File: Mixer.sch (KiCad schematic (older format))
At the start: 53 parts, among them J1 JST XH, J10 JST XH, J11 JST XH, J12 Conn_01x03_Female, J2 JST XH, J3 JST XH, J4 JST XH, J5 JST XH, J6 JST XH, J7 JST XH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

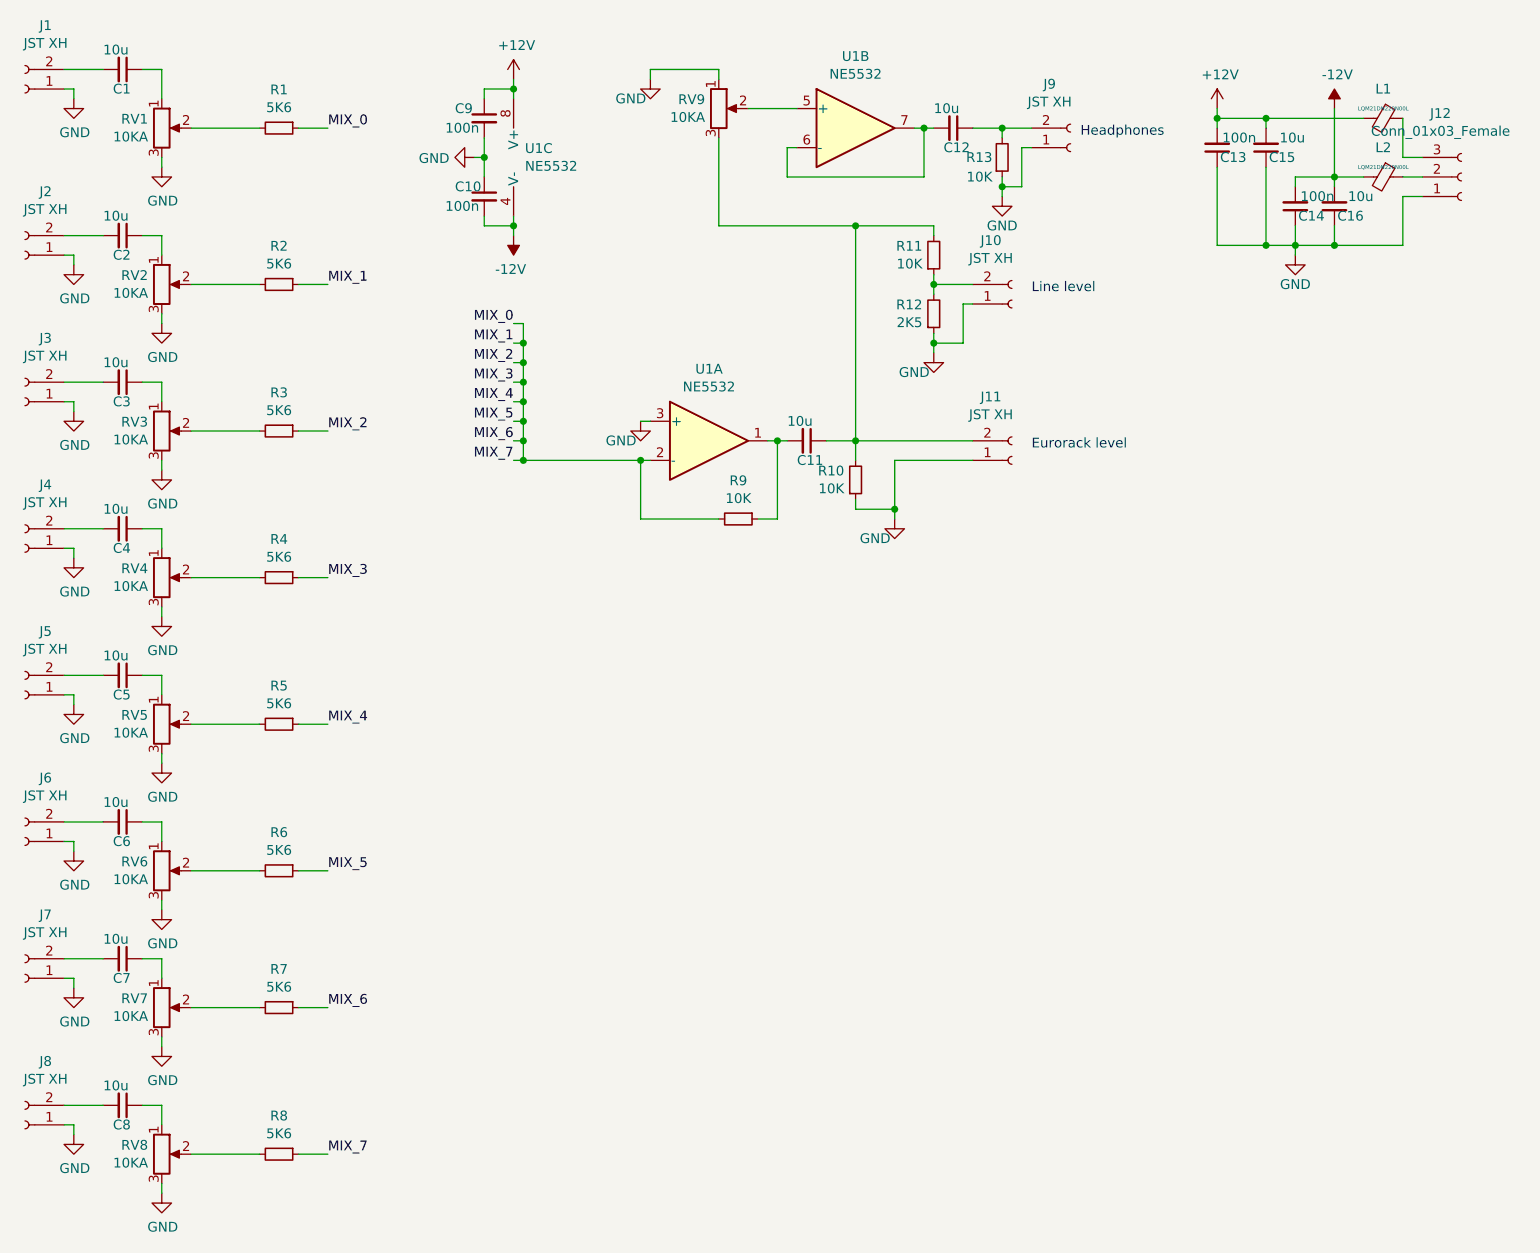
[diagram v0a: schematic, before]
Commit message: bugfix after prototype build
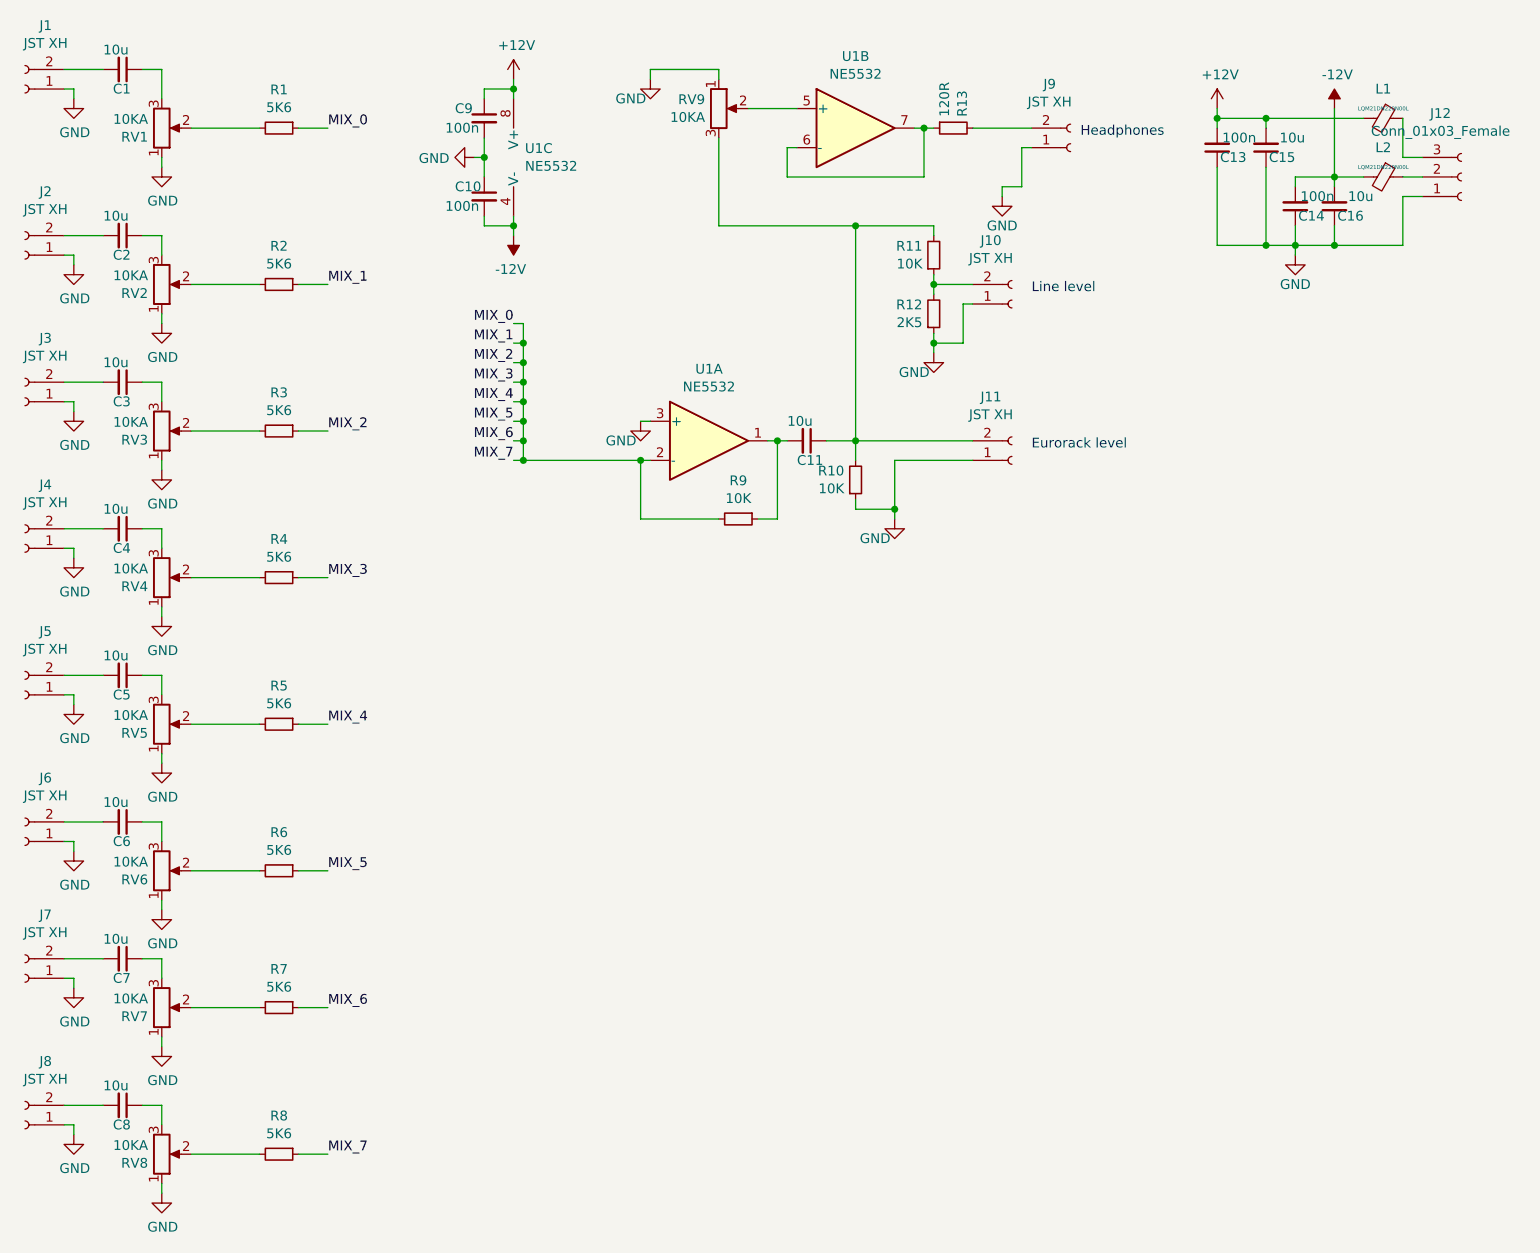
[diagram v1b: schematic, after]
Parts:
- removed C12: 10u, Capacitor_SMD:C_0805_2012Metric_Pad1.15x1.40mm_HandSolder, symbol Device:C_Small
- R13: value 10K -> 120R
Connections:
- net GND: now also RV1.1, RV2.1, RV3.1, RV4.1, RV5.1, RV6.1, RV7.1, RV8.1; no longer R13.1, RV1.3, RV2.3, RV3.3, RV4.3, RV5.3, RV6.3, RV7.3, RV8.3
- net at U1.6 (-), U1.7: now also R13.1
- net at C1.1: now also RV1.3; no longer RV1.1
- net at C2.1: now also RV2.3; no longer RV2.1
- net at C3.1: now also RV3.3; no longer RV3.1
- net at C4.1: now also RV4.3; no longer RV4.1
- net at C5.1: now also RV5.3; no longer RV5.1
- net at C6.1: now also RV6.3; no longer RV6.1
- net at C7.1: now also RV7.3; no longer RV7.1
- net at C8.1: now also RV8.3; no longer RV8.1
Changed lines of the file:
@@
 F 3 "~" H 1700 1000 50  0001 C CNN
 	1    1700 1000
-	1    0    0    -1
+	1    0    0    1
 $EndComp
 $Comp
@@
 F 3 "~" H 1700 1800 50  0001 C CNN
 	1    1700 1800
-	1    0    0    -1
+	1    0    0    1
 $EndComp
 $Comp
@@
 F 3 "~" H 1700 2550 50  0001 C CNN
 	1    1700 2550
-	1    0    0    -1
+	1    0    0    1
 $EndComp
 $Comp
@@
 F 3 "~" H 1700 3300 50  0001 C CNN
 	1    1700 3300
-	1    0    0    -1
+	1    0    0    1
 $EndComp
 $Comp
@@
 F 3 "~" H 1700 4050 50  0001 C CNN
 	1    1700 4050
-	1    0    0    -1
+	1    0    0    1
 $EndComp
 $Comp
@@
 F 3 "~" H 1700 4800 50  0001 C CNN
 	1    1700 4800
-	1    0    0    -1
+	1    0    0    1
 $EndComp
 $Comp
@@
 F 3 "~" H 1700 5500 50  0001 C CNN
 	1    1700 5500
-	1    0    0    -1
+	1    0    0    1
 $EndComp
 $Comp
@@
 F 3 "~" H 1700 6250 50  0001 C CNN
 	1    1700 6250
-	1    0    0    -1
+	1    0    0    1
 $EndComp
 $Comp
@@
 Wire Wire Line
 	1200 700  1400 700
-$Comp
-L Device:C_Small C12
-U 1 1 5B5B65D1
-P 5750 1000
-F 0 "C12" V 5850 950 50  0000 L CNN
-F 1 "10u" V 5650 900 50  0000 L CNN
-F 2 "Capacitor_SMD:C_0805_2012Metric_Pad1.15x1.40mm_HandSolder" H 5750 1000 50  0001 C CNN
-F 3 "~" H 5750 1000 50  0001 C CNN
-	1    5750 1000
-	0    1    1    0
-$EndComp
-Wire Wire Line
-	5650 1000 5600 1000
 Connection ~ 5600 1000
 $Comp
@@
 Wire Wire Line
 	7700 900  7700 1250
+Wire Wire Line
+	6000 1350 6000 1300
+Wire Wire Line
+	6150 1100 6100 1100
+Wire Wire Line
+	6100 1100 6100 1300
+Wire Wire Line
+	6100 1300 6000 1300
+Wire Wire Line
+	7700 1600 8050 1600
+Wire Wire Line
+	5850 1000 6150 1000
+Wire Wire Line
+	5650 1000 5600 1000
 $Comp
 L Device:R_Small R13
-U 1 1 5B5F4AE7
-P 6000 1150
-F 0 "R13" H 5950 1150 50  0000 R CNN
-F 1 "10K" H 5950 1250 50  0000 R CNN
-F 2 "Resistor_SMD:R_0805_2012Metric_Pad1.15x1.40mm_HandSolder" H 6000 1150 50  0001 C CNN
-F 3 "~" H 6000 1150 50  0001 C CNN
-	1    6000 1150
-	1    0    0    1
-$EndComp
-Wire Wire Line
-	5850 1000 6000 1000
-Wire Wire Line
-	6000 1350 6000 1300
-Wire Wire Line
-	6150 1100 6100 1100
-Wire Wire Line
-	6100 1100 6100 1300
-Wire Wire Line
-	6100 1300 6000 1300
-Connection ~ 6000 1300
-Wire Wire Line
-	6000 1300 6000 1250
-Wire Wire Line
-	6000 1050 6000 1000
-Connection ~ 6000 1000
-Wire Wire Line
-	6000 1000 6150 1000
-Wire Wire Line
-	7700 1600 8050 1600
+U 1 1 5C3BA133
+P 5750 1000
+F 0 "R13" H 5692 954 50  0000 R CNN
+F 1 "120R" H 5692 1045 50  0000 R CNN
+F 2 "Resistor_SMD:R_0805_2012Metric_Pad1.15x1.40mm_HandSolder" H 5750 1000 50  0001 C CNN
+F 3 "~" H 5750 1000 50  0001 C CNN
+	1    5750 1000
+	0    -1   1    0
+$EndComp
 $EndSCHEMATC
